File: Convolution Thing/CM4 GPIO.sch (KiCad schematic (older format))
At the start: 15 parts, among them J3 GPIO Header, U1 Compute_Module_4_Functional

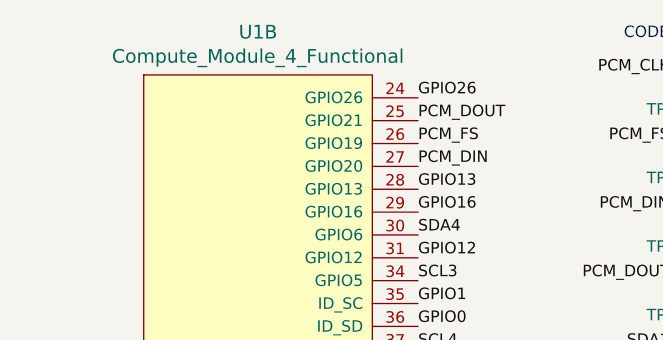
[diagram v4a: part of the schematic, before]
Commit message: Started footprint assignment
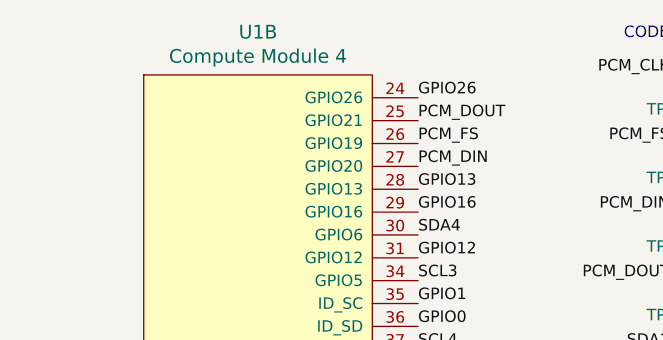
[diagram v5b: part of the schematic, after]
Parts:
- U1: value Compute_Module_4_Functional -> Compute Module 4; footprint (none) -> CM4:Raspberry-Pi-4-Compute-Module
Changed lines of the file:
@@
 P 900 1100
 F 0 "U1" H 1600 1387 60  0000 C CNN
-F 1 "Compute_Module_4_Functional" H 1600 1281 60  0000 C CNN
-F 2 "" H 1100 1150 60  0001 L CNN
+F 1 "Compute Module 4" H 1600 1281 60  0000 C CNN
+F 2 "CM4:Raspberry-Pi-4-Compute-Module" H 1100 1150 60  0001 L CNN
 F 3 "" H 1100 950 60  0001 L CNN
 	2    900  1100

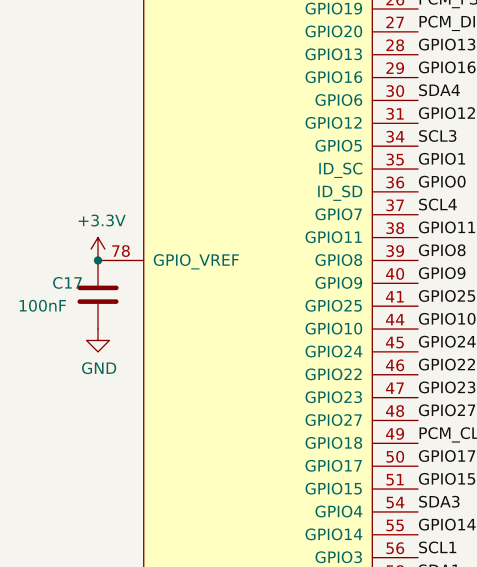
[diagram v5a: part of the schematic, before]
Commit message: Assign all footprints
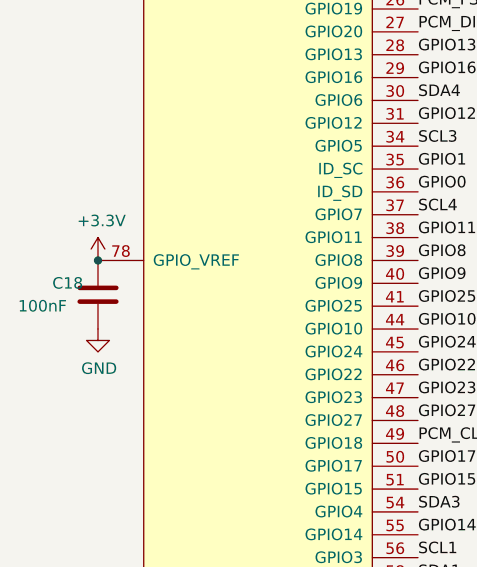
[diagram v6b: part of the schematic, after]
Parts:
- C18: renamed from C17; footprint (none) -> Capacitor_SMD:C_0805_2012Metric
- J3: footprint (none) -> Connector_PinSocket_2.54mm:PinSocket_1x15_P2.54mm_Vertical
- TP10, TP11, TP12, TP13, TP14, TP3, TP4, TP5, TP6, TP7, TP8, TP9: footprint (none) -> TestPoint:TestPoint_Loop_D2.60mm_Drill1.6mm_Beaded
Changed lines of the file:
@@
 $EndComp
 $Comp
-L power:+3.3V #PWR039
+L power:+3.3V #PWR040
 U 1 1 6108F224
 P 900 2400
-F 0 "#PWR039" H 900 2250 50  0001 C CNN
+F 0 "#PWR040" H 900 2250 50  0001 C CNN
 F 1 "+3.3V" H 915 2573 50  0000 C CNN
 F 2 "" H 900 2400 50  0001 C CNN
@@
 F 0 "TP3" H 3700 1150 50  0000 R CNN
 F 1 "PCM_CLK TP" H 3450 1150 50  0000 R CNN
-F 2 "" H 3700 1000 50  0001 C CNN
+F 2 "TestPoint:TestPoint_Loop_D2.60mm_Drill1.6mm_Beaded" H 3700 1000 50  0001 C CNN
 F 3 "~" H 3700 1000 50  0001 C CNN
 	1    3500 1000
@@
 F 0 "TP4" H 3700 1450 50  0000 R CNN
 F 1 "PCM_FS TP" H 3450 1450 50  0000 R CNN
-F 2 "" H 3700 1300 50  0001 C CNN
+F 2 "TestPoint:TestPoint_Loop_D2.60mm_Drill1.6mm_Beaded" H 3700 1300 50  0001 C CNN
 F 3 "~" H 3700 1300 50  0001 C CNN
 	1    3500 1300
@@
 F 0 "TP5" H 3700 1750 50  0000 R CNN
 F 1 "PCM_DIN TP" H 3450 1750 50  0000 R CNN
-F 2 "" H 3700 1600 50  0001 C CNN
+F 2 "TestPoint:TestPoint_Loop_D2.60mm_Drill1.6mm_Beaded" H 3700 1600 50  0001 C CNN
 F 3 "~" H 3700 1600 50  0001 C CNN
 	1    3500 1600
@@
 F 0 "TP6" H 3700 2050 50  0000 R CNN
 F 1 "PCM_DOUT TP" H 3450 2050 50  0000 R CNN
-F 2 "" H 3700 1900 50  0001 C CNN
+F 2 "TestPoint:TestPoint_Loop_D2.60mm_Drill1.6mm_Beaded" H 3700 1900 50  0001 C CNN
 F 3 "~" H 3700 1900 50  0001 C CNN
 	1    3500 1900
@@
 F 0 "TP7" H 3700 2350 50  0000 R CNN
 F 1 "CODEC_SDA TP" H 3450 2350 50  0000 R CNN
-F 2 "" H 3700 2200 50  0001 C CNN
+F 2 "TestPoint:TestPoint_Loop_D2.60mm_Drill1.6mm_Beaded" H 3700 2200 50  0001 C CNN
 F 3 "~" H 3700 2200 50  0001 C CNN
 	1    3500 2200
@@
 F 0 "TP8" H 3700 2650 50  0000 R CNN
 F 1 "CODEC_SCL TP" H 3450 2650 50  0000 R CNN
-F 2 "" H 3700 2500 50  0001 C CNN
+F 2 "TestPoint:TestPoint_Loop_D2.60mm_Drill1.6mm_Beaded" H 3700 2500 50  0001 C CNN
 F 3 "~" H 3700 2500 50  0001 C CNN
 	1    3500 2500
@@
 F 0 "TP9" H 4900 1150 50  0000 R CNN
 F 1 "DISPLAY_SCL TP" H 4650 1150 50  0000 R CNN
-F 2 "" H 4900 1000 50  0001 C CNN
+F 2 "TestPoint:TestPoint_Loop_D2.60mm_Drill1.6mm_Beaded" H 4900 1000 50  0001 C CNN
 F 3 "~" H 4900 1000 50  0001 C CNN
 	1    4700 1000
@@
 F 0 "TP10" H 4900 1450 50  0000 R CNN
 F 1 "DISPLAY_SDA TP" H 4650 1450 50  0000 R CNN
-F 2 "" H 4900 1300 50  0001 C CNN
+F 2 "TestPoint:TestPoint_Loop_D2.60mm_Drill1.6mm_Beaded" H 4900 1300 50  0001 C CNN
 F 3 "~" H 4900 1300 50  0001 C CNN
 	1    4700 1300
@@
 F 0 "TP11" H 6050 1150 50  0000 R CNN
 F 1 "CV_SCL TP" H 5800 1150 50  0000 R CNN
-F 2 "" H 6050 1000 50  0001 C CNN
+F 2 "TestPoint:TestPoint_Loop_D2.60mm_Drill1.6mm_Beaded" H 6050 1000 50  0001 C CNN
 F 3 "~" H 6050 1000 50  0001 C CNN
 	1    5850 1000
@@
 F 0 "TP12" H 6050 1450 50  0000 R CNN
 F 1 "CV_SDA TP" H 5800 1450 50  0000 R CNN
-F 2 "" H 6050 1300 50  0001 C CNN
+F 2 "TestPoint:TestPoint_Loop_D2.60mm_Drill1.6mm_Beaded" H 6050 1300 50  0001 C CNN
 F 3 "~" H 6050 1300 50  0001 C CNN
 	1    5850 1300
@@
 SCL3
 $Comp
-L Device:C C17
+L Device:C C18
 U 1 1 612C059D
 P 900 2550
-F 0 "C17" H 1100 2600 50  0000 R CNN
+F 0 "C18" H 1100 2600 50  0000 R CNN
 F 1 "100nF" H 1250 2500 50  0000 R CNN
-F 2 "" H 938 2400 50  0001 C CNN
+F 2 "Capacitor_SMD:C_0805_2012Metric" H 938 2400 50  0001 C CNN
 F 3 "~" H 900 2550 50  0001 C CNN
 	1    900  2550
@@
 Connection ~ 900  2400
 $Comp
-L power:GND #PWR040
+L power:GND #PWR041
 U 1 1 612C15EE
 P 900 2700
-F 0 "#PWR040" H 900 2450 50  0001 C CNN
+F 0 "#PWR041" H 900 2450 50  0001 C CNN
 F 1 "GND" H 905 2527 50  0000 C CNN
 F 2 "" H 900 2700 50  0001 C CNN
@@
 F 0 "TP13" H 7000 1150 50  0000 R CNN
 F 1 "CV_SCL TP" H 6750 1150 50  0000 R CNN
-F 2 "" H 7000 1000 50  0001 C CNN
+F 2 "TestPoint:TestPoint_Loop_D2.60mm_Drill1.6mm_Beaded" H 7000 1000 50  0001 C CNN
 F 3 "~" H 7000 1000 50  0001 C CNN
 	1    6800 1000
@@
 F 0 "TP14" H 7000 1450 50  0000 R CNN
 F 1 "CV_SDA TP" H 6750 1450 50  0000 R CNN
-F 2 "" H 7000 1300 50  0001 C CNN
+F 2 "TestPoint:TestPoint_Loop_D2.60mm_Drill1.6mm_Beaded" H 7000 1300 50  0001 C CNN
 F 3 "~" H 7000 1300 50  0001 C CNN
 	1    6800 1300
@@
 F 0 "J3" H 9228 1726 50  0000 L CNN
 F 1 "GPIO Header" H 9228 1635 50  0000 L CNN
-F 2 "" H 9200 1700 50  0001 C CNN
+F 2 "Connector_PinSocket_2.54mm:PinSocket_1x15_P2.54mm_Vertical" H 9200 1700 50  0001 C CNN
 F 3 "~" H 9200 1700 50  0001 C CNN
 	1    9200 1700
